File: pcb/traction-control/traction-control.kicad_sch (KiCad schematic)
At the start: 49 parts, among them J1 Conn_01x05_Socket, J2 Conn_01x04_Pin, J3 Screw_Terminal_01x06, J4 Conn_01x04_Pin, J5 Conn_ARM_SWD_TagConnect_TC203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, Q1 AO3400A, Q2 AO3401A, SW1 SW_Push, SW2 SW_Push, SW3 SW_Push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

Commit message: Revision and production files
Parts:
- added JP1: SolderJumper_3_Open, Jumper:SolderJumper-3_P1.3mm_Open_RoundedPad1.0x1.5mm, symbol Jumper:SolderJumper_3_Open
- C6: LCSC C15195 -> C1525
- R2: LCSC (none) -> C25900
- U1: LCSC (none) -> C6482
- renumbered C24 to C17, C17 to C18, D8 to D1, J5 to J3, J3 to J4, J4 to J5
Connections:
- net BTN1: now also U2.45 (PB8)
- net BTN2: now also U2.46 (PB9)
- net BTN3: now also U2.3 (PC14)
- net BTN4: now also U2.4 (PC15)
- net DRV1: now also U2.17 (PA7)
- net DRV2: now also U2.16 (PA6)
- net GPS_RX: now also U2.31 (PA10); no longer U2.13 (PA3)
- net GPS_TX: now also U2.30 (PA9); no longer U2.12 (PA2)
- net PGPS: now also U2.25 (PB12)
- net SCLD: now also U2.21 (PB10); no longer U2.42 (PB6)
- net SCLE: now also U2.42 (PB6); no longer U2.21 (PB10)
- net SDAD: now also U2.22 (PB11); no longer U2.43 (PB7)
- net SDAE: now also U2.43 (PB7); no longer U2.22 (PB11)
- net SIG1: now also U2.15 (PA5)
- net SIG2: now also U2.13 (PA3)
- net SNS1: now also JP1.3 (B); no longer J4.5 (Pin_5)
- net SNS2: now also JP1.1 (A); no longer J4.6 (Pin_6)
- net SIG3: now reaches U2.14 (PA4)
- new net: J4.6 (Pin_6), JP1.2 (C)
- new net SNS3: J4.5 (Pin_5)
- no-connect marks 2 -> 18
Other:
- removed sheet Input1
- added sheet Sensor2 (sensor.kicad_sch)
- added sheet Tac1 (tac.kicad_sch)
- sheet Sensor1 ports: added OUT; removed SIG
- moved on the sheet: J4

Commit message: Save
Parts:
- Q1: LCSC (none) -> C20917
- Q2: LCSC (none) -> C15127
- R1, R6: LCSC (none) -> C25744
- R7: LCSC (none) -> C25890
- U3: LCSC (none) -> C6186
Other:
- moved on the sheet: C10
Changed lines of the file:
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@@
 	(paper "A4")
 	(junction
+		(at 245.11 85.09)
+		(diameter 0)
+		(color 0 0 0 0)
+	)
+	(junction
 		(at 226.06 43.18)
 		(diameter 0)
@@
 	)
 	(junction
-		(at 247.65 85.09)
-		(diameter 0)
-		(color 0 0 0 0)
-	)
-	(junction
 		(at 238.76 53.34)
 		(diameter 0)
@@
 	(wire
 		(pts
-			(xy 247.65 82.55) (xy 247.65 85.09)
+			(xy 245.11 82.55) (xy 245.11 85.09)
 		)
 		(stroke
@@
 	(wire
 		(pts
-			(xy 247.65 95.25) (xy 247.65 97.79)
+			(xy 245.11 95.25) (xy 245.11 97.79)
 		)
 		(stroke
@@
 	(wire
 		(pts
-			(xy 247.65 87.63) (xy 247.65 85.09)
+			(xy 245.11 87.63) (xy 245.11 85.09)
 		)
 		(stroke
@@
 	(wire
 		(pts
+			(xy 245.11 85.09) (xy 252.73 85.09)
+		)
+		(stroke
+			(width 0)
+			(type default)
+		)
+	)
+	(wire
+		(pts
 			(xy 241.3 154.94) (xy 243.84 154.94)
 		)
@@
 		)
 	)
-	(wire
-		(pts
-			(xy 247.65 85.09) (xy 252.73 85.09)
-		)
-		(stroke
-			(width 0)
-			(type default)
-		)
-	)
 	(polyline
 		(pts
@@
 	(wire
 		(pts
-			(xy 247.65 97.79) (xy 260.35 97.79)
+			(xy 245.11 97.79) (xy 260.35 97.79)
 		)
 		(stroke
@@
 			)
 		)
+		(property "LCSC" "C25744"
+			(at 271.78 133.35 0)
+			(effects
+				(font
+					(size 1.27 1.27)
+				)
+				(hide yes)
+			)
+		)
 		(pin "1"
 		)
@@
 	(symbol
 		(lib_id "Device:C")
-		(at 247.65 91.44 0)
+		(at 245.11 91.44 0)
 		(unit 1)
 		(exclude_from_sim no)
@@
 		(fields_autoplaced yes)
 		(property "Reference" "C10"
-			(at 251.46 90.1699 0)
+			(at 248.92 90.1699 0)
 			(effects
 				(font
@@
 		)
 		(property "Value" "22u"
-			(at 251.46 92.7099 0)
+			(at 248.92 92.7099 0)
 			(effects
 				(font
@@
 		)
 		(property "Footprint" "Capacitor_SMD:C_0805_2012Metric"
-			(at 248.6152 95.25 0)
+			(at 246.0752 95.25 0)
 			(effects
 				(font
@@
 		)
 		(property "Datasheet" "~"
-			(at 247.65 91.44 0)
+			(at 245.11 91.44 0)
 			(effects
 				(font
@@
 		)
 		(property "Description" "Unpolarized capacitor"
-			(at 247.65 91.44 0)
+			(at 245.11 91.44 0)
 			(effects
 				(font
@@
 		)
 		(property "LCSC" "C45783"
-			(at 247.65 91.44 0)
+			(at 245.11 91.44 0)
 			(effects
 				(font
@@
 			)
 		)
+		(property "LCSC" "C25744"
+			(at 154.94 29.21 90)
+			(effects
+				(font
+					(size 1.27 1.27)
+				)
+				(hide yes)
+			)
+		)
 		(pin "2"
 		)
@@
 			)
 		)
+		(property "LCSC" "C15127"
+			(at 148.59 36.83 90)
+			(effects
+				(font
+					(size 1.27 1.27)
+				)
+				(hide yes)
+			)
+		)
 		(pin "1"
 		)
@@
 			)
 		)
+		(property "LCSC" "C25890"
+			(at 271.78 146.05 0)
+			(effects
+				(font
+					(size 1.27 1.27)
+				)
+				(hide yes)
+			)
+		)
 		(pin "1"
 		)
@@
 			)
 		)
+		(property "LCSC" "C6186"
+			(at 260.35 85.09 0)
+			(effects
+				(font
+					(size 1.27 1.27)
+				)
+				(hide yes)
+			)
+		)
 		(pin "3"
 		)
@@
 	(symbol
 		(lib_id "power:+5V")
-		(at 247.65 82.55 0)
+		(at 245.11 82.55 0)
 		(unit 1)
 		(exclude_from_sim no)
@@
 		(fields_autoplaced yes)
 		(property "Reference" "#PWR017"
-			(at 247.65 86.36 0)
+			(at 245.11 86.36 0)
 			(effects
 				(font
@@
 		)
 		(property "Value" "+5V"
-			(at 247.65 77.47 0)
+			(at 245.11 77.47 0)
 			(effects
 				(font
@@
 		)
 		(property "Footprint" ""
-			(at 247.65 82.55 0)
+			(at 245.11 82.55 0)
 			(effects
 				(font
@@
 		)
 		(property "Datasheet" ""
-			(at 247.65 82.55 0)
+			(at 245.11 82.55 0)
 			(effects
 				(font
@@
 		)
 		(property "Description" "Power symbol creates a global label with name \"+5V\""
-			(at 247.65 82.55 0)
+			(at 245.11 82.55 0)
 			(effects
 				(font
@@
 			(at 130.81 36.83 0)
 			(effects
+				(font
+					(size 1.27 1.27)
+				)
+				(hide yes)
+			)
+		)
+		(property "LCSC" "C20917"
+			(at 130.81 36.83 0)
+			(effects

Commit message: Make production files
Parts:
- removed J5: Conn_01x04_Pin, Connector_PinHeader_2.54mm:PinHeader_1x04_P2.54mm_Vertical, symbol Connector:Conn_01x04_Pin
- removed U2: STM32F103C8Tx, Package_QFP:LQFP-48_7x7mm_P0.5mm, symbol MCU_ST_STM32F1:STM32F103C8Tx
- added C19: 10n, Capacitor_SMD:C_0402_1005Metric, symbol Device:C
- added C20, C21: 1u, Capacitor_SMD:C_0402_1005Metric, symbol Device:C
- added C22: 47u, Capacitor_SMD:C_1206_3216Metric, symbol Device:C
- added FB1: 100, Inductor_SMD:L_0805_2012Metric, symbol Device:FerriteBead
- added U2: STM32G431CBTx, Package_QFP:LQFP-48_7x7mm_P0.5mm, symbol MCU_ST_STM32G4:STM32G431CBTx
- added U5: SSD1306, User_Footprints:SSD1309_1.3, symbol User_Symbols:SSD1306_128x64
- C2, C3, C4, C5, C7: LCSC (none) -> C1525
- C8, C9: LCSC (none) -> C32949
- J4: footprint TerminalBlock:TerminalBlock_bornier-6_P5.08mm -> User_Footprints:ScrewTerminalPlug_6P_P5.08
- R3: LCSC (none) -> C25900
- R4, R8, R9: LCSC (none) -> C25744
- Y1: LCSC (none) -> C13738
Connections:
- net SNS3 is gone; now on net SNS1: J4.5 (Pin_5)
- net +3V3: now also C21.1, FB1.2, U2.1 (VBAT), U2.24 (VDD), U2.36 (VDD), U2.48 (VDD), U5.2 (VCC)
- net BOOT0: now also U2.45 (PB8)
- net BTN1: now also U2.2 (PC13)
- net BTN2: now also U2.42 (PB5)
- net BTN3: now also U2.13 (PA5)
- net BTN4: now also U2.18 (PB2)
- net DRV1: now also U2.26 (PB12)
- net DRV2: now also U2.25 (PB11)
- net GND: now also C19.2, C20.2, C21.2, C22.2, U2.19 (VSSA), U2.23 (VSS), U2.35 (VSS), U2.47 (VSS), U5.1 (GND)
- net GPS_RX: now also U2.44 (PB7)
- net GPS_TX: now also U2.43 (PB6)
- net PGPS: now also U2.33 (PA11)
- net RST: now also U2.7 (PG10)
- net SCLD: now also U2.31 (PA9), U5.3 (SCL)
- net SCLE: now also U2.39 (PA15)
- net SDAD: now also U2.30 (PA8), U5.4 (SDA)
- net SDAE: now also U2.46 (PB9)
- net SIG1: now also U2.11 (PA3)
- net SIG2: now also U2.9 (PA1)
- net SNS1: no longer JP1.3 (B)
- net SNS2: now also JP1.3 (B); no longer JP1.1 (A)
- net SWCLK: now also U2.38 (PA14)
- net SWDIO: now also U2.37 (PA13)
- net SWO: now also U2.40 (PB3)
- net XTALI: now also U2.5 (PF0)
- net XTALO: now also U2.6 (PF1)
- net at J1.1 (Pin_1), Q2.2 (S), R1.2: now also C22.1
- new net +3V3A: C19.1, C20.1, FB1.1, U2.20 (VREF+), U2.21 (VDDA)
- new net SNST: JP1.1 (A)
- new net TACH: U2.16 (PB0), U2.8 (PA0)
- no-connect marks 18 -> 16
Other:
- moved on the sheet: C1, C18, C2, C3, C4, C5, J1, J2, J4, JP1, Q1, Q2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

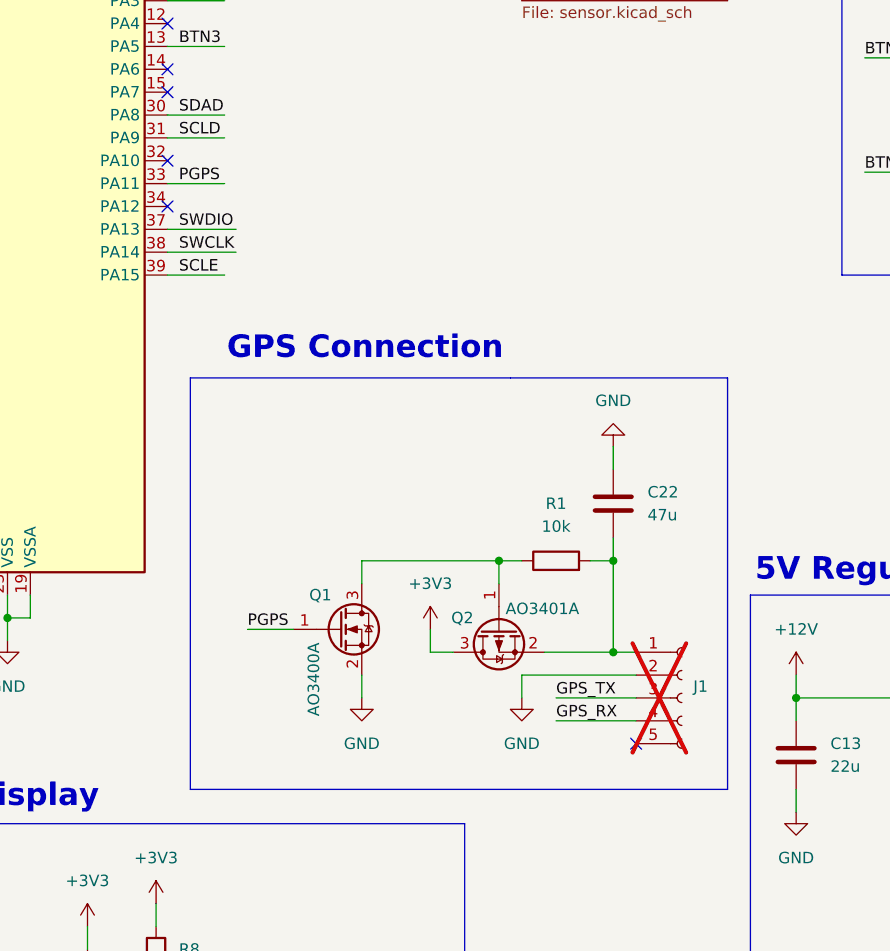
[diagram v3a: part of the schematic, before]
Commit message: Fix power connection
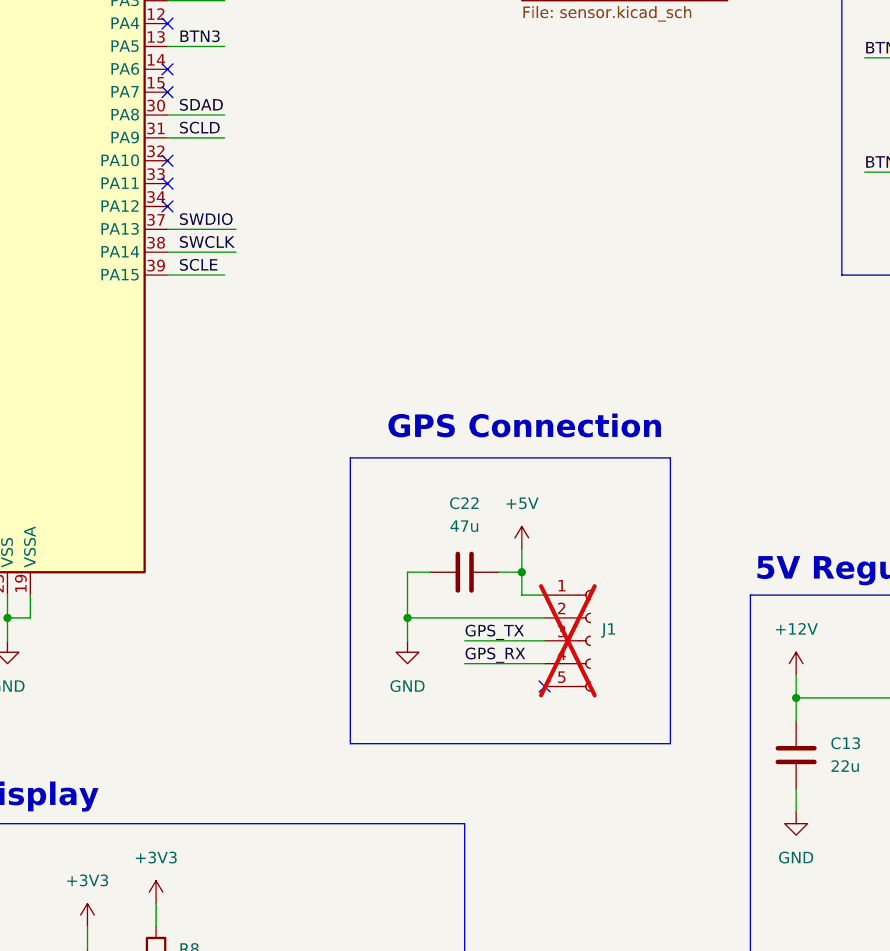
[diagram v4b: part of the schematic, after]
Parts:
- removed Q1: AO3400A, Package_TO_SOT_SMD:SOT-23, symbol Transistor_FET:AO3400A
- removed Q2: AO3401A, Package_TO_SOT_SMD:SOT-23, symbol Transistor_FET:AO3401A
- removed R1: 10k, Resistor_SMD:R_0402_1005Metric, symbol Device:R
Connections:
- net +5V: now also C22.1, J1.1 (Pin_1)
- net PGPS: no longer names the net of U2.33 (PA11)
- no-connect marks 16 -> 17
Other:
- moved on the sheet: C22, J1
